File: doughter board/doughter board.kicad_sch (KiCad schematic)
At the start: 36 parts, among them J301 RS485, J304 SWD, J305 BOOT_TO/ SELECTOR, J306 UART2, J311 BOOT_TO/ SELECTOR, SW301 SW_SPST, U301 SN65HVD11, U302 LM1117-3.3, U303 STM32F030C6Tx, Y301 8 MHz

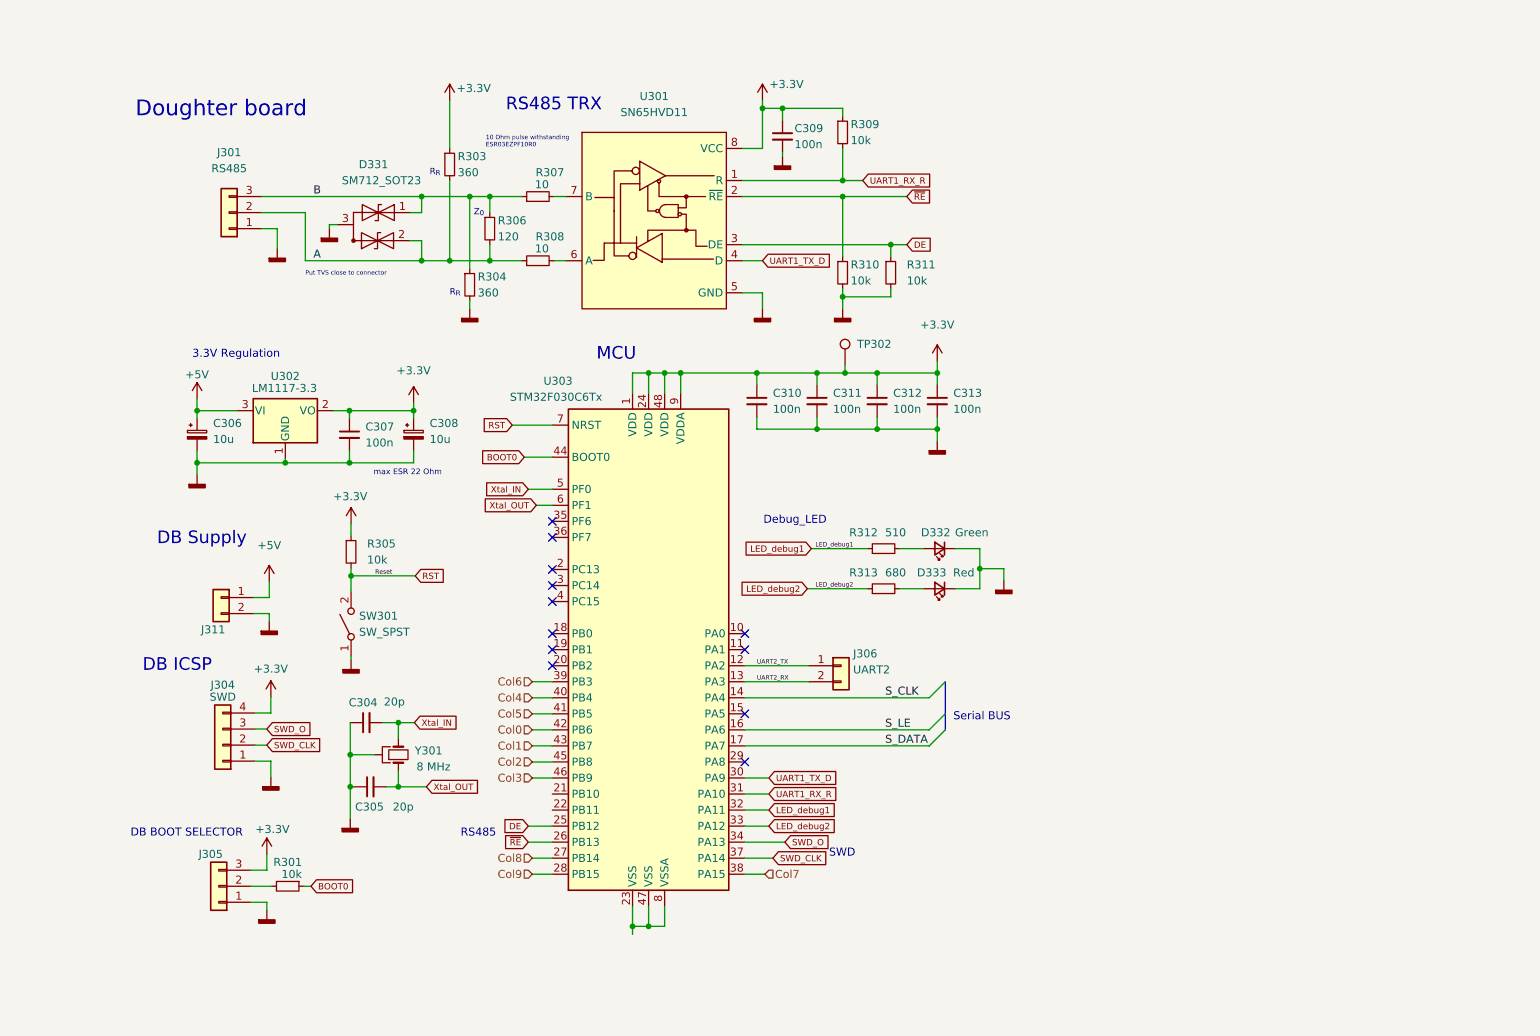
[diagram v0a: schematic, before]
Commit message: finished schematic of daughter board
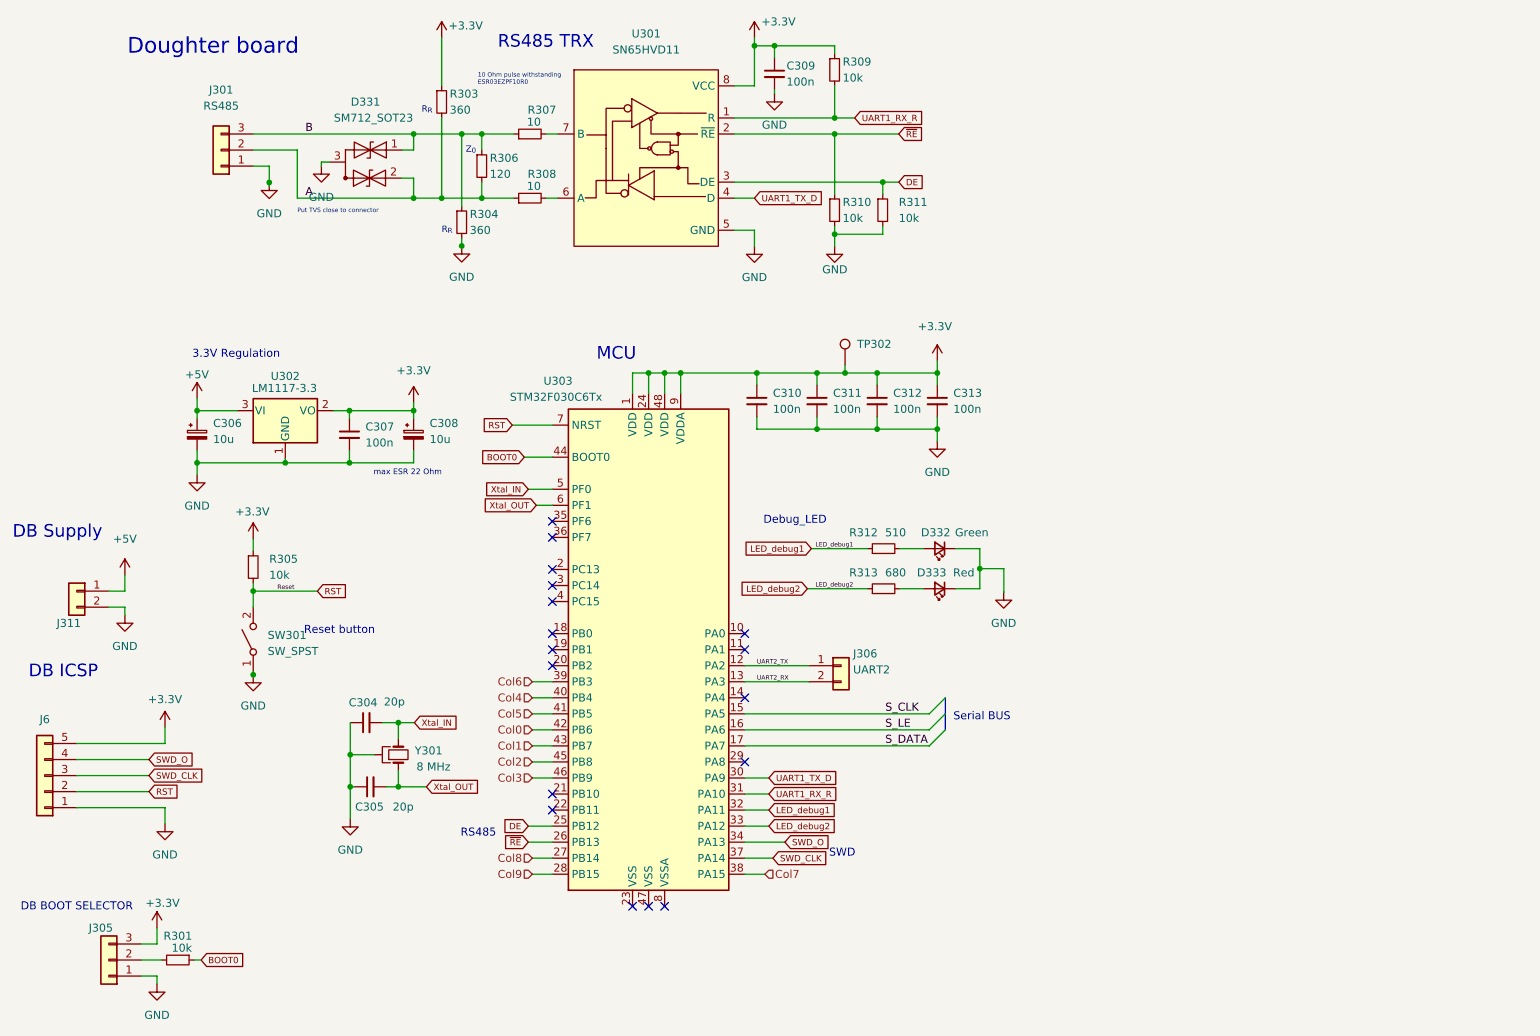
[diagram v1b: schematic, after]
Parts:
- removed J304: SWD, Connector_PinSocket_2.54mm:PinSocket_1x04_P2.54mm_Vertical_SMD_Pin1Right, symbol Connector_Generic:Conn_01x04
- added J6: Conn_01x05, symbol Connector_Generic:Conn_01x05
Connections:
- net +3.3V: now also J6.5 (Pin_5)
- net RST: now also J6.2 (Pin_2)
- net SWD_CLK: now also J6.3 (Pin_3)
- net SWD_O: now also J6.4 (Pin_4)
- net S_CLK: now also U303.15 (PA5); no longer U303.14 (PA4)
- net GNDD renamed GND
- net GND: now also J6.1 (Pin_1)
- now unconnected: U303.23 (VSS), U303.47 (VSS), U303.8 (VSSA)
- no-connect marks 12 -> 17
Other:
- note added: "Reset button"
- moved on the sheet: C309, D331, J301, J305, J311, R301, R303, R304, R305, R306, R307, R308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

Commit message: br
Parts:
- J3: renamed from J6; footprint (none) -> Connector_PinSocket_2.54mm:PinSocket_1x05_P2.54mm_Vertical
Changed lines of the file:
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@@
   (symbol (lib_id "Connector_Generic:Conn_01x05") (at 19.05 137.16 180) (unit 1)
     (in_bom yes) (on_board yes) (dnp no)
-    (property "Reference" "J6" (at 19.05 128.27 0)
+    (property "Reference" "J3" (at 19.05 128.27 0)
       (effects (font (size 1.27 1.27)))
     )
@@
       (effects (font (size 1.27 1.27)) hide)
     )
-    (property "Footprint" "" (at 19.05 137.16 0)
+    (property "Footprint" "Connector_PinSocket_2.54mm:PinSocket_1x05_P2.54mm_Vertical" (at 19.05 137.16 0)
       (effects (font (size 1.27 1.27)) hide)
     )
@@
       (project "doughter board"
         (path "/1ea1a0ba-623e-4676-8b59-1c632e7c560a"
-          (reference "J6") (unit 1)
+          (reference "J3") (unit 1)
         )
       )

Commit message: cd.
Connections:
- net at U303.23 (VSS): now also U303.47 (VSS), U303.8 (VSSA)
- no-connect marks 17 -> 14
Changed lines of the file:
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@@
   (junction (at 150.876 82.296) (diameter 0) (color 0 0 0 0)
+  )
+  (junction (at 114.681 157.861) (diameter 0) (color 0 0 0 0)
   )
   (junction (at 43.18 87.63) (diameter 0) (color 0 0 0 0)
@@
   (no_connect (at 99.441 96.901))
   (no_connect (at 129.921 135.001))
-  (no_connect (at 117.221 157.861))
   (no_connect (at 129.921 117.221))
   (no_connect (at 99.441 140.081))
-  (no_connect (at 112.141 157.861))
   (no_connect (at 99.441 104.521))
   (no_connect (at 99.441 142.621))
   (no_connect (at 99.441 99.441))
   (no_connect (at 129.921 114.681))
-  (no_connect (at 114.681 157.861))
   (no_connect (at 99.441 109.601))
   (no_connect (at 99.441 114.681))
@@
     (stroke (width 0) (type default))
   )
+  (wire (pts (xy 114.681 157.861) (xy 117.221 157.861))
+    (stroke (width 0) (type default))
+  )
   (wire (pts (xy 144.145 35.56) (xy 144.145 45.085))
     (stroke (width 0) (type default))
@@
     (stroke (width 0) (type default))
   )
+  (wire (pts (xy 112.141 157.861) (xy 114.681 157.861))
+    (stroke (width 0) (type default))
+  )

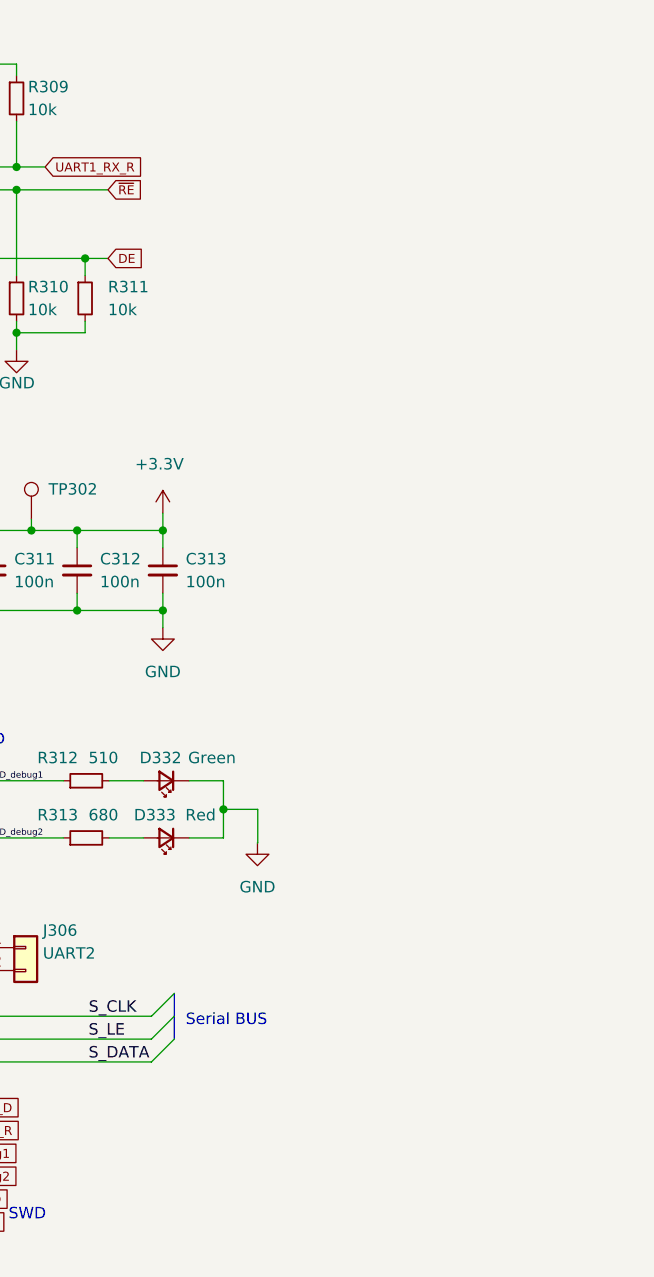
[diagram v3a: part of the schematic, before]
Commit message: doughter PCB - with no GND connection
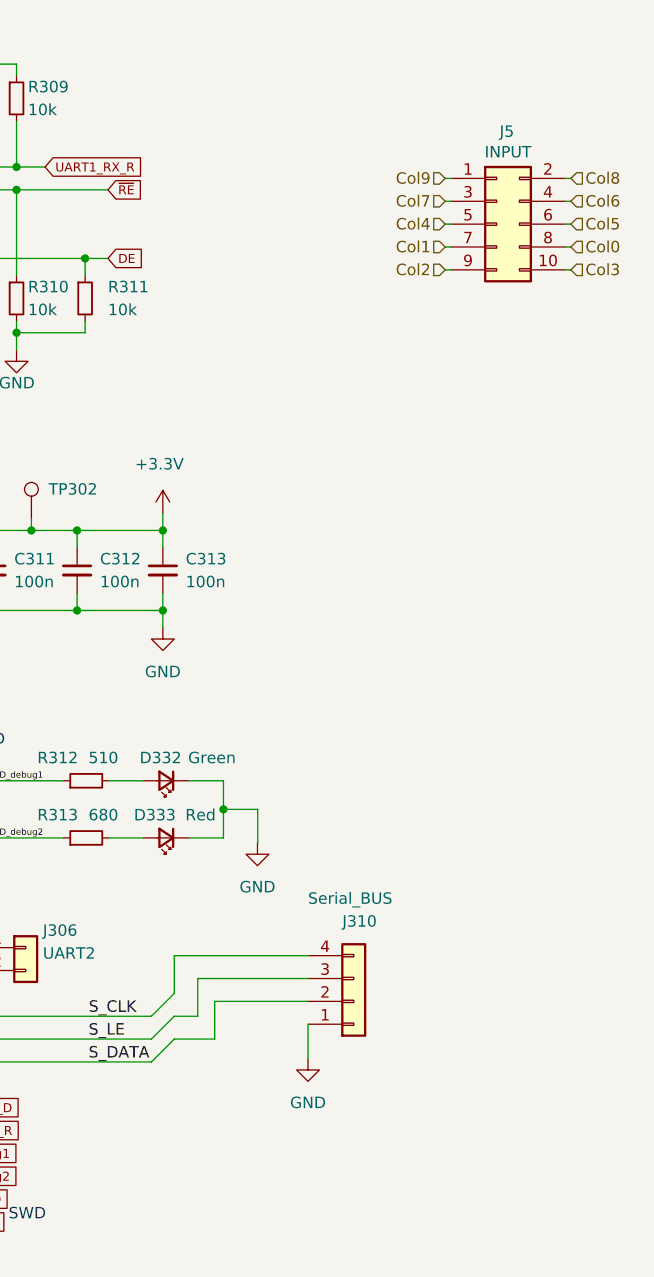
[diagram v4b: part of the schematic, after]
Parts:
- added J310: Serial_BUS, Connector_PinSocket_2.54mm:PinSocket_1x04_P2.54mm_Vertical_SMD_Pin1Right, symbol Connector_Generic:Conn_01x04
- added J5: INPUT, Connector_PinHeader_2.54mm:PinHeader_2x05_P2.54mm_Vertical_SMD, symbol Connector_Generic:Conn_02x05_Odd_Even
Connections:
- net Col0: now also J5.8 (Pin_8)
- net Col1: now also J5.7 (Pin_7)
- net Col2: now also J5.9 (Pin_9)
- net Col3: now also J5.10 (Pin_10)
- net Col4: now also J5.5 (Pin_5)
- net Col5: now also J5.6 (Pin_6)
- net Col6: now also J5.4 (Pin_4)
- net Col7: now also J5.3 (Pin_3)
- net Col8: now also J5.2 (Pin_2)
- net Col9: now also J5.1 (Pin_1)
- net GND: now also J310.1 (Pin_1)
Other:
- note removed: "Serial BUS"

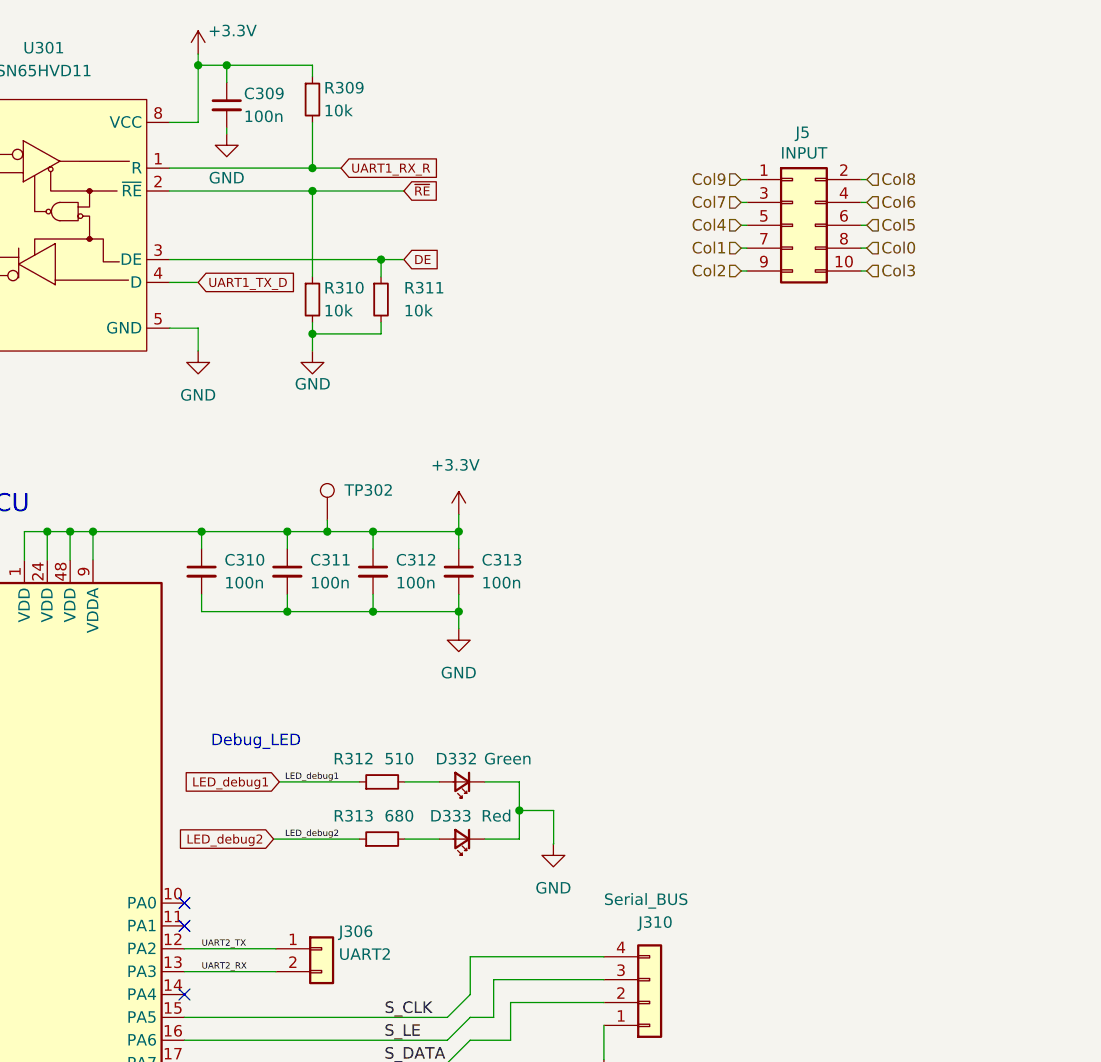
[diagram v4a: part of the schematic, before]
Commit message: Modified layout, filled GND planes, added info on silkscreen
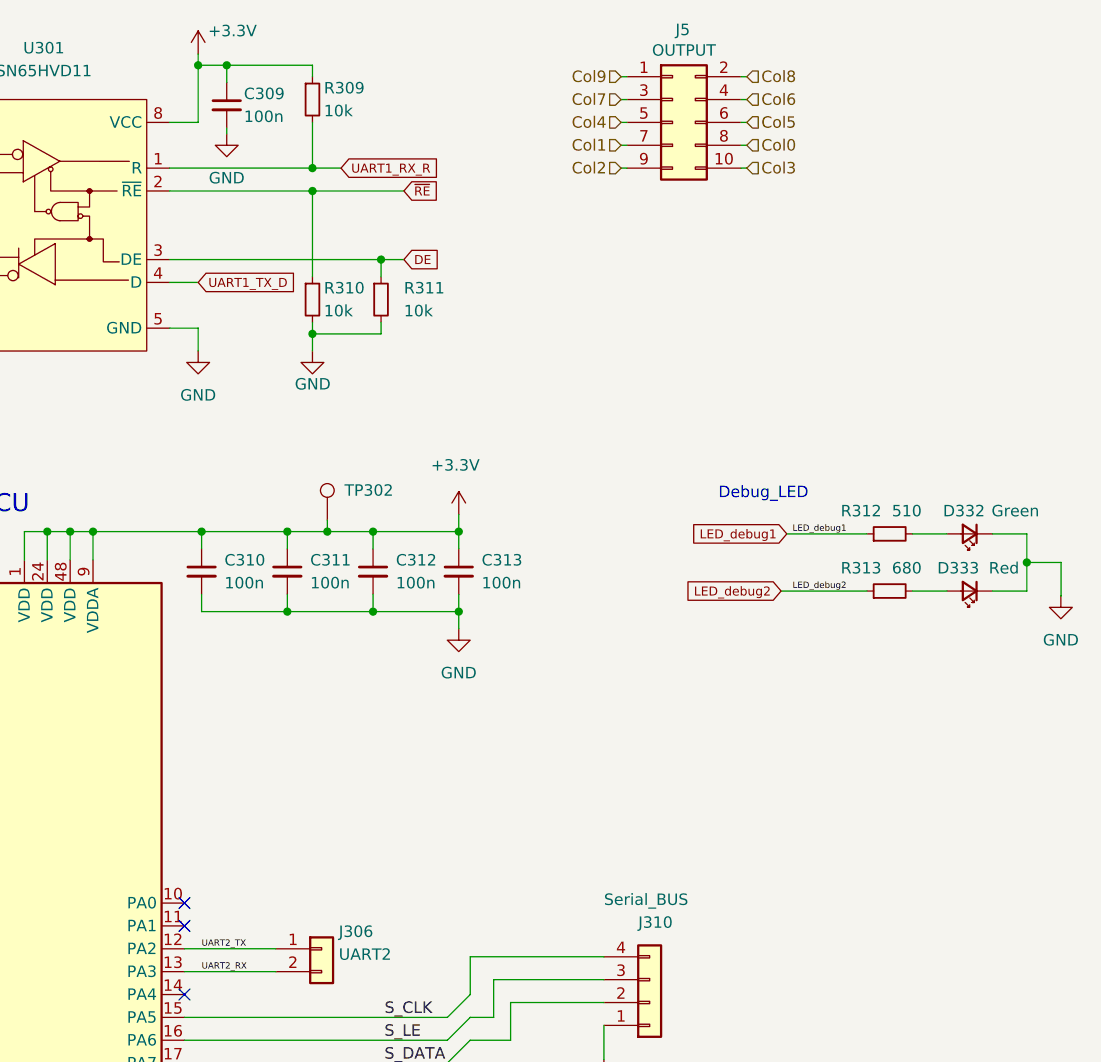
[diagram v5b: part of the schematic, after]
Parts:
- J3: footprint Connector_PinSocket_2.54mm:PinSocket_1x05_P2.54mm_Vertical -> Connector_PinSocket_2.54mm:PinSocket_1x05_P2.54mm_Vertical_SMD_Pin1Left
- J5: value INPUT -> OUTPUT
- TP302: footprint TestPoint:TestPoint_Pad_2.0x2.0mm -> TestPoint:TestPoint_Pad_1.0x1.0mm
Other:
- moved on the sheet: D332, D333, J5, R312, R313
